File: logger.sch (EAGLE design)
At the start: 73 parts, among them IC1 LTC4412, J1 POWER_JACKPTH, Q1 FDN360P, Q2 FDN360P, Q5 2N7002PW, U3 FT231XS

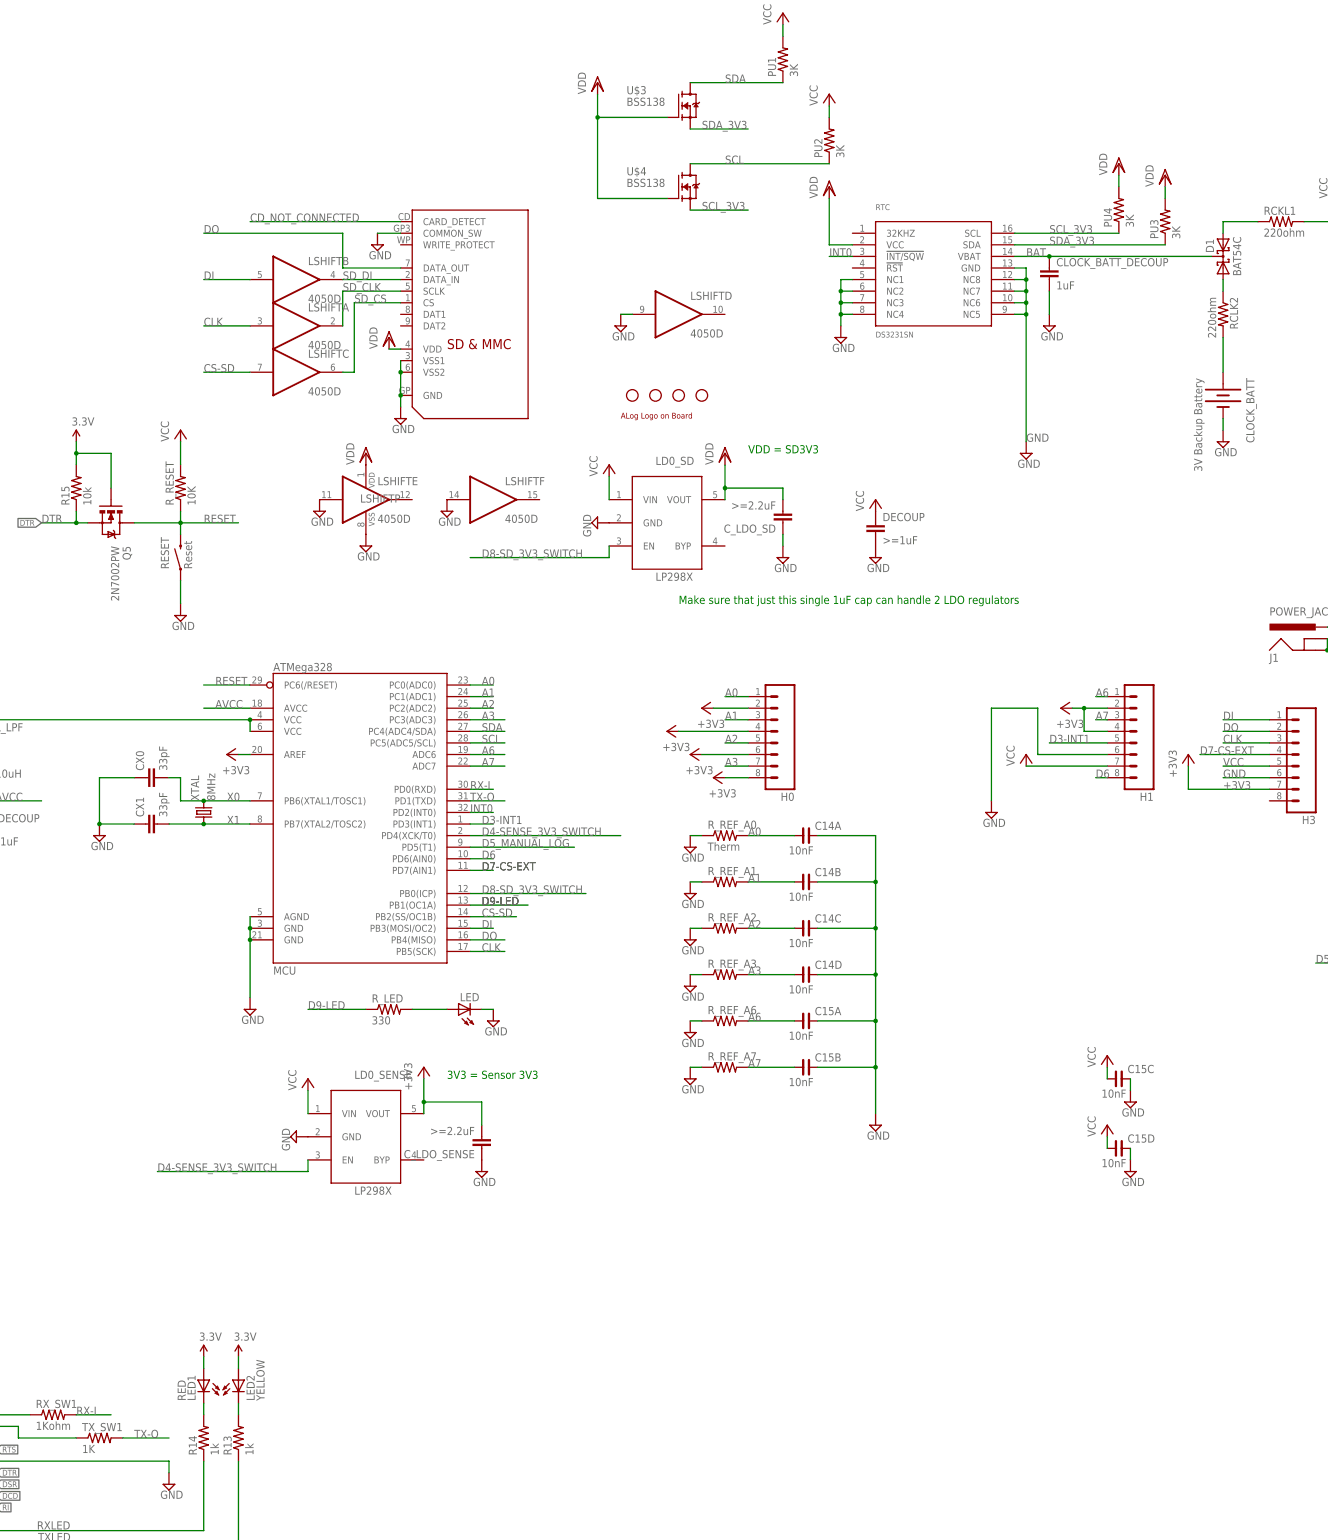
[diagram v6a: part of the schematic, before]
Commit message: Uniform MOSFETs; diode connection fix
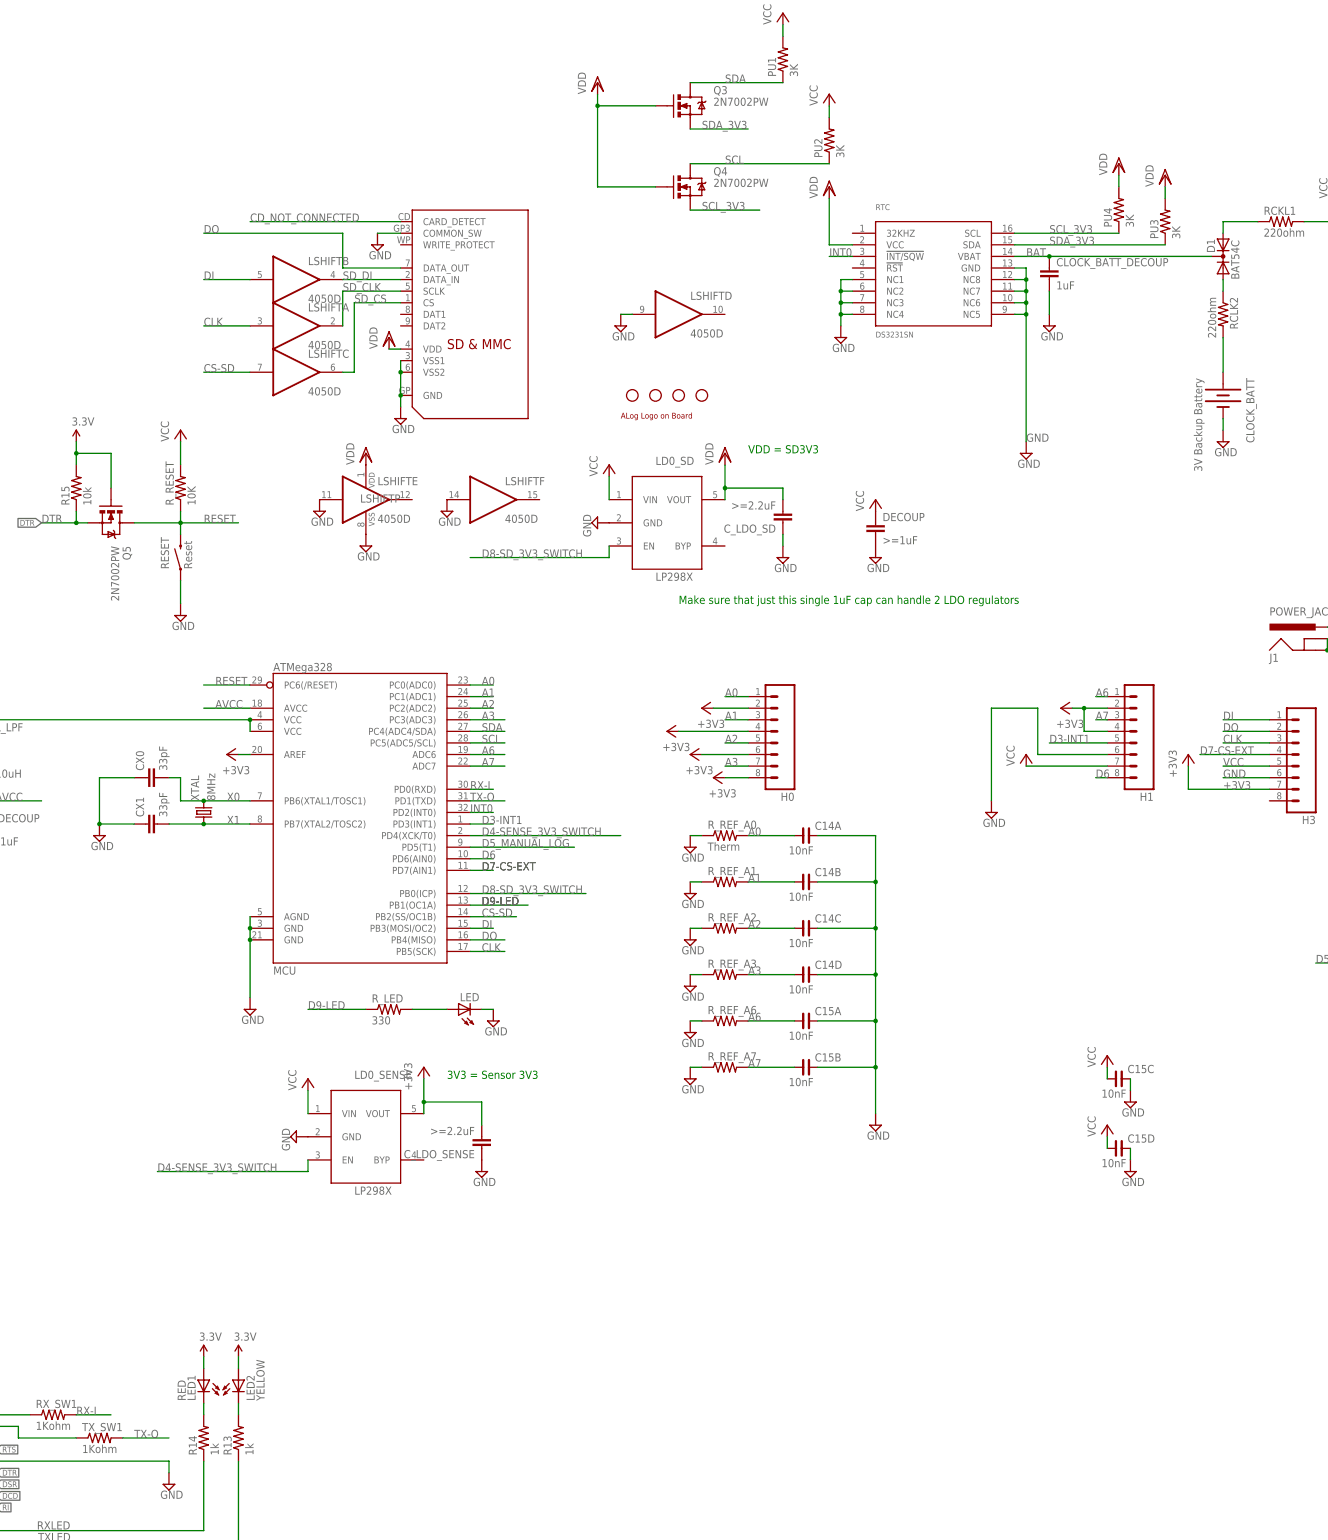
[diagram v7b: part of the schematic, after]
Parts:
- removed U$3, U$4: BSS138, SteveMarple:BSS138SOT23-3-HAND
- added Q3, Q4: 2N7002PW, SparkFun-DiscreteSemi:MOSFET-NCHANNELSOT323
- D1: device diode:BAT54C -> semicon-smd-ipc:DIODE_AC-CA_
- TX_SW1: value 1K -> 1Kohm
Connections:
- removed net N$68: D1.CC
- net BAT: now also D1.K
- net SCL: now also Q4.D; no longer U$4.D
- net SCL_3V3: now also Q4.S; no longer U$4.S
- net SDA: now also Q3.D; no longer U$3.D
- net SDA_3V3: now also Q3.S; no longer U$3.S
- net VDD: now also Q3.G, Q4.G; no longer U$3.G, U$4.G
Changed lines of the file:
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@@
 <part name="CLOCK_BATT_DECOUP" library="rcl" deviceset="C-EU" device="C0603" value="1uF"/>
 <part name="SUPPLY47" library="supply2" deviceset="GND" device=""/>
-<part name="D1" library="diode" deviceset="BAT54C" device=""/>
+<part name="D1" library="semicon-smd-ipc" deviceset="DIODE_AC-CA_" device="" value="BAT54C"/>
 <part name="SUPPLY39" library="supply2" deviceset="GND" device=""/>
 <part name="SUPPLY40" library="supply2" deviceset="GND" device=""/>
@@
 <part name="U$10" library="MyPOW" deviceset="VUSB" device=""/>
 <part name="RX_SW1" library="rcl" deviceset="R-US_" device="R0603" value="1Kohm"/>
-<part name="TX_SW1" library="rcl" deviceset="R-US_" device="R0603" value="1K"/>
+<part name="TX_SW1" library="rcl" deviceset="R-US_" device="R0603" value="1Kohm"/>
 <part name="SUPPLY44" library="supply2" deviceset="GND" device=""/>
 <part name="SUPPLY45" library="supply2" deviceset="GND" device=""/>
@@
 <part name="P+10" library="supply1" deviceset="VCC" device=""/>
 <part name="SD_3V4" library="supply1" deviceset="VDD" device=""/>
-<part name="U$3" library="SteveMarple" deviceset="BSS138" device="SOT23-3-HAND" value="BSS138"/>
-<part name="U$4" library="SteveMarple" deviceset="BSS138" device="SOT23-3-HAND" value="BSS138"/>
 <part name="PU3" library="rcl" deviceset="R-US_" device="R0603" value="3K"/>
 <part name="PU4" library="rcl" deviceset="R-US_" device="R0603" value="3K"/>
@@
 <part name="P+12" library="supply1" deviceset="VCC" device=""/>
 <part name="P+13" library="supply1" deviceset="VCC" device=""/>
+<part name="Q3" library="SparkFun-DiscreteSemi" deviceset="MOSFET-NCHANNEL" device="SOT323" value="2N7002PW"/>
+<part name="Q4" library="SparkFun-DiscreteSemi" deviceset="MOSFET-NCHANNEL" device="SOT323" value="2N7002PW"/>
 </parts>
 <sheets>
@@
 <instance part="P+10" gate="VCC" x="342.9" y="231.14"/>
 <instance part="SD_3V4" gate="G$1" x="231.14" y="231.14"/>
-<instance part="U$3" gate="G$1" x="200.66" y="248.92"/>
-<instance part="U$4" gate="G$1" x="200.66" y="231.14"/>
 <instance part="PU3" gate="G$1" x="304.8" y="223.52" rot="R90"/>
 <instance part="PU4" gate="G$1" x="294.64" y="226.06" rot="R90"/>
@@
 <instance part="P+12" gate="VCC" x="231.14" y="251.46"/>
 <instance part="P+13" gate="VCC" x="220.98" y="269.24"/>
+<instance part="Q3" gate="G$1" x="200.66" y="248.92"/>
+<instance part="Q4" gate="G$1" x="200.66" y="231.14"/>
 </instances>
 <busses>
@@
 </segment>
 <segment>
-<pinref part="U$4" gate="G$1" pin="D"/>
 <wire x1="200.66" y1="236.22" x2="231.14" y2="236.22" width="0.1524" layer="91"/>
 <label x="208.28" y="236.22" size="1.778" layer="95"/>
 <pinref part="PU2" gate="G$1" pin="1"/>
+<pinref part="Q4" gate="G$1" pin="D"/>
 </segment>
 </net>
@@
 </segment>
 <segment>
-<pinref part="U$3" gate="G$1" pin="D"/>
 <wire x1="200.66" y1="254" x2="220.98" y2="254" width="0.1524" layer="91"/>
 <label x="208.28" y="254" size="1.778" layer="95"/>
 <pinref part="PU1" gate="G$1" pin="1"/>
+<pinref part="Q3" gate="G$1" pin="D"/>
 </segment>
 </net>
@@
 <pinref part="RTC" gate="G$1" pin="VBAT"/>
 <pinref part="CLOCK_BATT_DECOUP" gate="G$1" pin="1"/>
-<wire x1="279.4" y1="215.9" x2="281.94" y2="215.9" width="0.1524" layer="91"/>
+<pinref part="D1" gate="G$1" pin="K"/>
+<wire x1="279.4" y1="215.9" x2="314.96" y2="215.9" width="0.1524" layer="91"/>
 <junction x="279.4" y="215.9"/>
 </segment>
@@
 </segment>
 <segment>
-<pinref part="U$4" gate="G$1" pin="G"/>
-<wire x1="195.58" y1="228.6" x2="180.34" y2="228.6" width="0.1524" layer="91"/>
-<wire x1="180.34" y1="228.6" x2="180.34" y2="246.38" width="0.1524" layer="91"/>
-<pinref part="U$3" gate="G$1" pin="G"/>
-<wire x1="180.34" y1="246.38" x2="180.34" y2="251.46" width="0.1524" layer="91"/>
-<wire x1="195.58" y1="246.38" x2="180.34" y2="246.38" width="0.1524" layer="91"/>
-<junction x="180.34" y="246.38"/>
+<wire x1="193.04" y1="231.14" x2="180.34" y2="231.14" width="0.1524" layer="91"/>
+<wire x1="180.34" y1="231.14" x2="180.34" y2="248.92" width="0.1524" layer="91"/>
+<wire x1="180.34" y1="248.92" x2="180.34" y2="251.46" width="0.1524" layer="91"/>
+<wire x1="193.04" y1="248.92" x2="180.34" y2="248.92" width="0.1524" layer="91"/>
+<junction x="180.34" y="248.92"/>
 <pinref part="SD_3V7" gate="G$1" pin="VDD"/>
+<pinref part="Q3" gate="G$1" pin="G"/>
+<pinref part="Q4" gate="G$1" pin="G"/>
 </segment>
 </net>
@@
 </segment>
 </net>
-<net name="N$68" class="0">
-<segment>
-<pinref part="D1" gate="G$1" pin="CC"/>
-<wire x1="314.96" y1="215.9" x2="281.94" y2="215.9" width="0.1524" layer="91"/>
-</segment>
-</net>
 <net name="N$27" class="0">
 <segment>
@@
 </segment>
 <segment>
-<pinref part="U$4" gate="G$1" pin="S"/>
-<wire x1="200.66" y1="226.06" x2="213.36" y2="226.06" width="0.1524" layer="91"/>
+<wire x1="200.66" y1="226.06" x2="215.9" y2="226.06" width="0.1524" layer="91"/>
 <label x="203.2" y="226.06" size="1.778" layer="95"/>
+<pinref part="Q4" gate="G$1" pin="S"/>
 </segment>
 </net>
@@
 </segment>
 <segment>
-<pinref part="U$3" gate="G$1" pin="S"/>
 <wire x1="200.66" y1="243.84" x2="213.36" y2="243.84" width="0.1524" layer="91"/>
 <label x="203.2" y="243.84" size="1.778" layer="95"/>
-</segment>
-</net>
+<pinref part="Q3" gate="G$1" pin="S"/>
+</segment>
+</net>

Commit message: ALog 1.1 complete
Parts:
- added U$3: NWLOGO_MED, awickert:NWLOGO_MED
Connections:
- removed net CD_NOT_CONNECTED: SD.CARD_DETECT
- removed net DCD: U3.!DCD
- removed net DSR: U3.!DSR
- removed net RI: U3.!RI
- removed net RTS: U3.!RTS
- net VCC: no longer C15D.1
- net VDD: now also C15D.1
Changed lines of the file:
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@@
 </variantdefs>
 <classes>
-<class number="0" name="default" width="0" drill="0">
+<class number="0" name="default" width="0.2032" drill="0.3048">
 </class>
-<class number="1" name="power" width="0.254" drill="0">
+<class number="1" name="power" width="0.3048" drill="0.508">
 </class>
-<class number="2" name="gnd" width="0.6096" drill="1">
+<class number="2" name="gnd" width="0.6096" drill="0.508">
 <clearance class="2" value="0.2032"/>
 </class>
@@
 <part name="SUPPLY38" library="supply2" deviceset="GND" device=""/>
 <part name="P+17" library="supply1" deviceset="VCC" device=""/>
-<part name="P+22" library="supply1" deviceset="VCC" device=""/>
 <part name="U3" library="SparkFun-DigitalIC" deviceset="FT231X" device="S"/>
 <part name="C17" library="SparkFun-Capacitors" deviceset="CAP" device="0402-CAP" value="0.1uF"/>
@@
 <part name="Q3" library="SparkFun-DiscreteSemi" deviceset="MOSFET-NCHANNEL" device="SOT323" value="2N7002PW"/>
 <part name="Q4" library="SparkFun-DiscreteSemi" deviceset="MOSFET-NCHANNEL" device="SOT323" value="2N7002PW"/>
+<part name="U$3" library="awickert" deviceset="NWLOGO_MED" device=""/>
+<part name="SD_3V8" library="supply1" deviceset="VDD" device=""/>
 </parts>
 <sheets>
@@
 <instance part="SUPPLY38" gate="GND" x="297.18" y="30.48"/>
 <instance part="P+17" gate="VCC" x="292.1" y="40.64"/>
-<instance part="P+22" gate="VCC" x="292.1" y="25.4"/>
 <instance part="U3" gate="G$1" x="33.02" y="-53.34"/>
 <instance part="C17" gate="G$1" x="27.94" y="-22.86"/>
@@
 <instance part="Q3" gate="G$1" x="200.66" y="248.92"/>
 <instance part="Q4" gate="G$1" x="200.66" y="231.14"/>
+<instance part="U$3" gate="G$1" x="-5.08" y="220.98"/>
+<instance part="SD_3V8" gate="G$1" x="292.1" y="25.4"/>
 </instances>
 <busses>
@@
 <wire x1="292.1" y1="35.56" x2="292.1" y2="38.1" width="0.1524" layer="91"/>
 <pinref part="P+17" gate="VCC" pin="VCC"/>
-</segment>
-<segment>
-<pinref part="C15" gate="D" pin="1"/>
-<wire x1="292.1" y1="20.32" x2="292.1" y2="22.86" width="0.1524" layer="91"/>
-<pinref part="P+22" gate="VCC" pin="VCC"/>
 </segment>
 <segment>
@@
 <net name="DTR" class="0">
 <segment>
-<pinref part="U3" gate="G$1" pin="!DTR"/>
-<wire x1="45.72" y1="-50.8" x2="48.26" y2="-50.8" width="0.1524" layer="91"/>
-<label x="48.26" y="-50.8" size="1.27" layer="95" xref="yes"/>
-<label x="58.42" y="157.48" size="1.27" layer="95" rot="R180" xref="yes"/>
-</segment>
-<segment>
 <pinref part="Q5" gate="G$1" pin="S"/>
 <pinref part="R15" gate="G$1" pin="1"/>
@@
 <junction x="66.04" y="157.48"/>
 <label x="58.42" y="157.48" size="1.778" layer="95"/>
+</segment>
+<segment>
+<pinref part="U3" gate="G$1" pin="!DTR"/>
+<wire x1="45.72" y1="-50.8" x2="53.34" y2="-50.8" width="0.1524" layer="91"/>
+<label x="48.26" y="-50.8" size="1.778" layer="95"/>
 </segment>
 </net>
@@
 </segment>
 </net>
-<net name="CD_NOT_CONNECTED" class="0">
-<segment>
-<wire x1="137.16" y1="223.52" x2="104.14" y2="223.52" width="0.1524" layer="91"/>
-<label x="104.14" y="223.52" size="1.778" layer="95"/>
-<pinref part="SD" gate="G$1" pin="CARD_DETECT"/>
-</segment>
-</net>
 <net name="D8-SD_3V3_SWITCH" class="0">
 <segment>
@@
 <pinref part="Q3" gate="G$1" pin="G"/>
 <pinref part="Q4" gate="G$1" pin="G"/>
+</segment>
+<segment>
+<pinref part="C15" gate="D" pin="1"/>
+<wire x1="292.1" y1="20.32" x2="292.1" y2="22.86" width="0.1524" layer="91"/>
+<pinref part="SD_3V8" gate="G$1" pin="VDD"/>
 </segment>
 </net>
@@
 <junction x="10.16" y="127"/>
 <pinref part="IC1" gate="G$1" pin="STAT"/>
-</segment>
-</net>
-<net name="RTS" class="0">
-<segment>
-<pinref part="U3" gate="G$1" pin="!RTS"/>
-<wire x1="45.72" y1="-45.72" x2="48.26" y2="-45.72" width="0.1524" layer="91"/>
-<label x="48.26" y="-45.72" size="1.27" layer="95" xref="yes"/>
-</segment>
-</net>
-<net name="DSR" class="0">
-<segment>
-<pinref part="U3" gate="G$1" pin="!DSR"/>
-<wire x1="45.72" y1="-53.34" x2="48.26" y2="-53.34" width="0.1524" layer="91"/>
-<label x="48.26" y="-53.34" size="1.27" layer="95" xref="yes"/>
-</segment>
-</net>
-<net name="DCD" class="0">
-<segment>
-<pinref part="U3" gate="G$1" pin="!DCD"/>
-<wire x1="45.72" y1="-55.88" x2="48.26" y2="-55.88" width="0.1524" layer="91"/>
-<label x="48.26" y="-55.88" size="1.27" layer="95" xref="yes"/>
-</segment>
-</net>
-<net name="RI" class="0">
-<segment>
-<pinref part="U3" gate="G$1" pin="!RI"/>
-<wire x1="45.72" y1="-58.42" x2="48.26" y2="-58.42" width="0.1524" layer="91"/>
-<label x="48.26" y="-58.42" size="1.27" layer="95" xref="yes"/>
 </segment>
 </net>
@@
 </sheet>
 </sheets>
+<errors>
+</errors>
 </schematic>
 </drawing>
